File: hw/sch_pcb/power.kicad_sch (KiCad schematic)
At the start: 15 parts, among them J1 HEADER_2x01, J2 HEADER_2x01_PARALLEL, J3 HEADER_2x01_PARALLEL, U8 TPS613222ADBV

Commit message: update ustid
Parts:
- C29, C52: UST_ID (none) -> 5c70984412875079b91f880f
- C32, C54, C55: UST_ID (none) -> 5c70984712875079b91f8b4c
- C36, C42, C50: UST_ID (none) -> 5c70984712875079b91f8b53
- D3: UST_ID (none) -> 5c70984512875079b91f88b2
- F2: UST_ID (none) -> 5cac42d21287500e61c241e5
- J1, J2, J3: now left out of the parts list
- L3: UST_ID (none) -> 5cc3309d128750448e54e8d8
- U8: UST_ID (none) -> 5c7190ae1287500b4e112e04

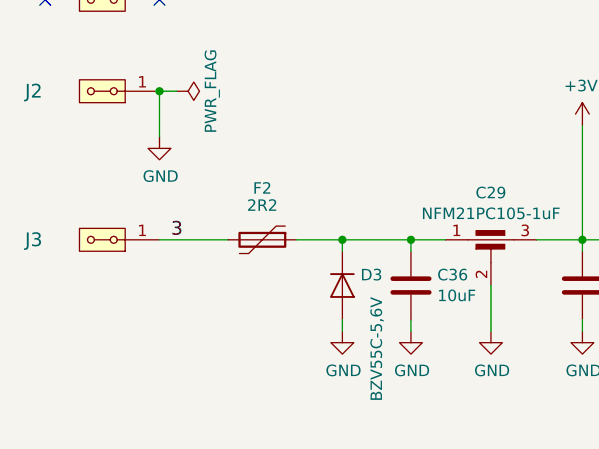
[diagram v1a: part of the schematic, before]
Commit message: Improve schematics desription.
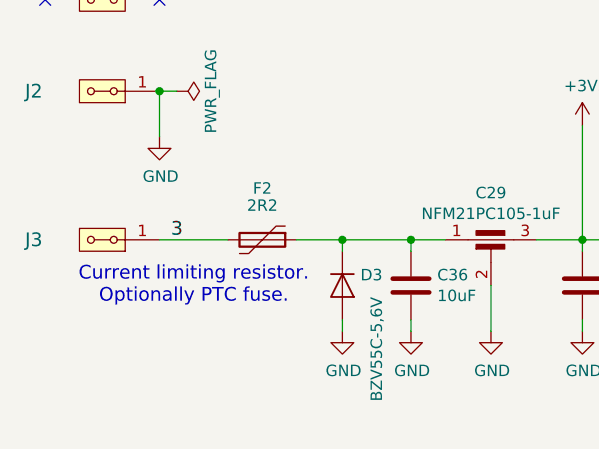
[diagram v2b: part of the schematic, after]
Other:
- note added: "Current limiting resistor. Optionally PTC fuse."
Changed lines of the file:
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@@
 		(comment 3 "Universal Scientific Technologies s.r.o. ")
+	)
+	(text "Current limiting resistor.\nOptionally PTC fuse. "
+		(exclude_from_sim no)
+		(at 54.61 90.17 0)
+		(effects
+			(font
+				(size 1.524 1.524)
+			)
+		)
 	)
 	(junction
